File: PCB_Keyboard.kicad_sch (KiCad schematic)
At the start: 14 parts, among them SW1 SW_Push, U1 ATmega32U4-A, Y1 16MHz

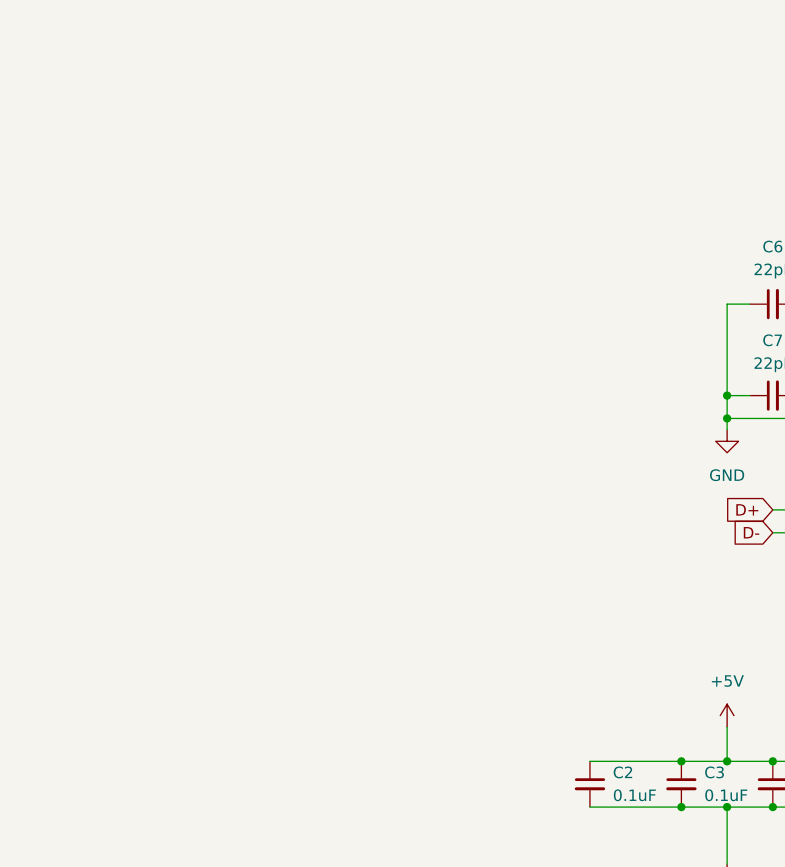
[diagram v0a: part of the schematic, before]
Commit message: Finalizando a Esquemática
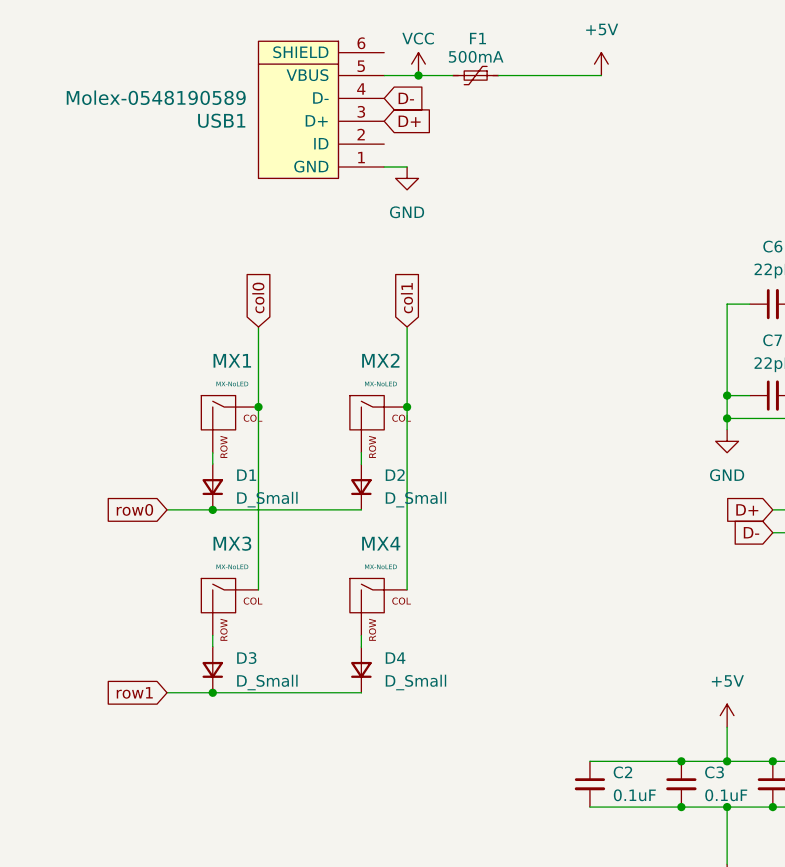
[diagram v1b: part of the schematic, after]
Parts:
- added D1, D2, D3, D4: D_Small, Diode_SMD:D_SOD-123, symbol Device:D_Small
- added F1: 500mA, Fuse:Fuse_1206_3216Metric, symbol Device:Polyfuse_Small
- added MX1, MX2, MX3, MX4: MX-NoLED, MX_Alps_Hybrid:MX-Alps-Hybrid-1U, symbol MX_Alps_Hybrid:MX-NoLED
- added USB1: Molex-0548190589, random-keyboard-parts:Molex-0548190589, symbol random-keyboard-parts:Molex-0548190589
- C1, C2, C3, C4, C5, C6, C7: footprint (none) -> Capacitor_SMD:C_0805_2012Metric
- R1, R2, R3, R4: footprint (none) -> Resistor_SMD:R_0805_2012Metric
- SW1: footprint (none) -> random-keyboard-parts:SKQG-1155865
- Y1: footprint (none) -> Crystal:Crystal_SMD_3225-4Pin_3.2x2.5mm
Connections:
- net +5V: now also F1.1
- net D+: now also USB1.3 (D+)
- net D-: now also USB1.4 (D-)
- net GND: now also USB1.1 (GND)
- new net: D2.2 (A), MX2.2 (ROW)
- new net: D4.2 (A), MX4.2 (ROW)
- new net: D1.2 (A), MX1.2 (ROW)
- new net: D3.2 (A), MX3.2 (ROW)
- new net VCC: F1.2, USB1.5 (VBUS)
- new net col0: MX1.1 (COL), MX3.1 (COL)
- new net col1: MX2.1 (COL), MX4.1 (COL)
- new net row0: D1.1 (K), D2.1 (K)
- new net row1: D3.1 (K), D4.1 (K)

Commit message: roteamento
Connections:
- net col0: now also U1.28 (PB4)
- net col1: now also U1.29 (PB5)
- net row0: now also U1.27 (PD7)
- net row1: now also U1.26 (PD6)
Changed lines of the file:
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@@
 	(global_label "col1"
 		(shape input)
+		(at 154.94 69.85 0)
+		(fields_autoplaced yes)
+		(effects
+			(font
+				(size 1.27 1.27)
+			)
+			(justify left)
+		)
+		(property "Intersheetrefs" "${INTERSHEET_REFS}"
+			(at 162.0375 69.85 0)
+			(effects
+				(font
+					(size 1.27 1.27)
+				)
+				(justify left)
+				(hide yes)
+			)
+		)
+	)
+	(global_label "col1"
+		(shape input)
 		(at 58.42 62.23 90)
 		(fields_autoplaced yes)
@@
 	(global_label "col0"
 		(shape input)
+		(at 154.94 67.31 0)
+		(fields_autoplaced yes)
+		(effects
+			(font
+				(size 1.27 1.27)
+			)
+			(justify left)
+		)
+		(property "Intersheetrefs" "${INTERSHEET_REFS}"
+			(at 162.0375 67.31 0)
+			(effects
+				(font
+					(size 1.27 1.27)
+				)
+				(justify left)
+				(hide yes)
+			)
+		)
+	)
+	(global_label "col0"
+		(shape input)
 		(at 41.91 62.23 90)
 		(fields_autoplaced yes)
@@
 			(effects
 				(font
+					(size 1.27 1.27)
+				)
+				(justify left)
+				(hide yes)
+			)
+		)
+	)
+	(global_label "row1"
+		(shape input)
+		(at 154.94 102.87 0)
+		(fields_autoplaced yes)
+		(effects
+			(font
+				(size 1.27 1.27)
+			)
+			(justify left)
+		)
+		(property "Intersheetrefs" "${INTERSHEET_REFS}"
+			(at 162.4004 102.87 0)
+			(effects
+				(font
+					(size 1.27 1.27)
+				)
+				(justify left)
+				(hide yes)
+			)
+		)
+	)
+	(global_label "row0"
+		(shape input)
+		(at 154.94 105.41 0)
+		(fields_autoplaced yes)
+		(effects
+			(font
+				(size 1.27 1.27)
+			)
+			(justify left)
+		)
+		(property "Intersheetrefs" "${INTERSHEET_REFS}"
+			(at 162.4004 105.41 0)
+			(effects
+				(font
